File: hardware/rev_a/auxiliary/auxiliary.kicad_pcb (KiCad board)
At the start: 4 copper layers, 90 x 75 mm, 52 parts, among them J101 K1_NUMBERED_SOLDER_TAILS, J102 DEVKIT_J1_NUMBERED_TAILS, J103 ADAFRUIT_5335_TAILS, J104 B6B-XH-A(LF)(SN), J105 REGULATED_5V_TAILS, J106 REMOTE_NO_STOP_CONTACT, U101 ISO7721DR, U102 TXU0304PWR, U103 TXU0304PWR, U104 TXU0304PWR, U105 TPS3703A4330DSER, U106 TPS3703A4330DSER, U107 TPS3703A5500DSER, U108 TPS3703A5500DSER, U109 SN74LVC1G97DBVR, U110 SN74LVC1G97DBVR, U111 SN74LVC2G74DCUR

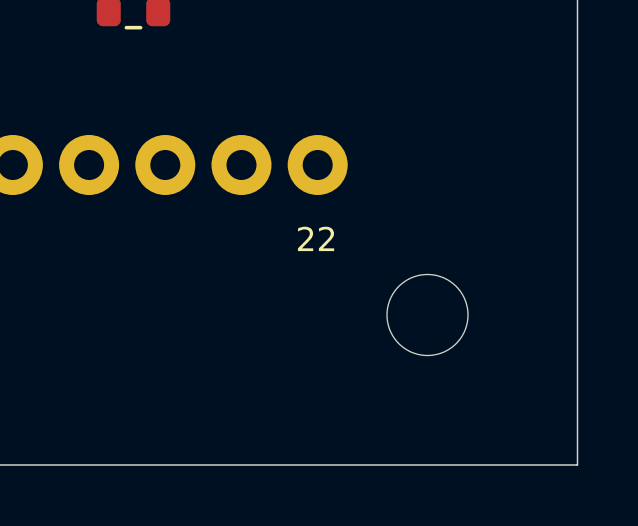
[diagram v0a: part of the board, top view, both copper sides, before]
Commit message: fix(hardware): move H4 clear of the unchanged MCU termination allocation
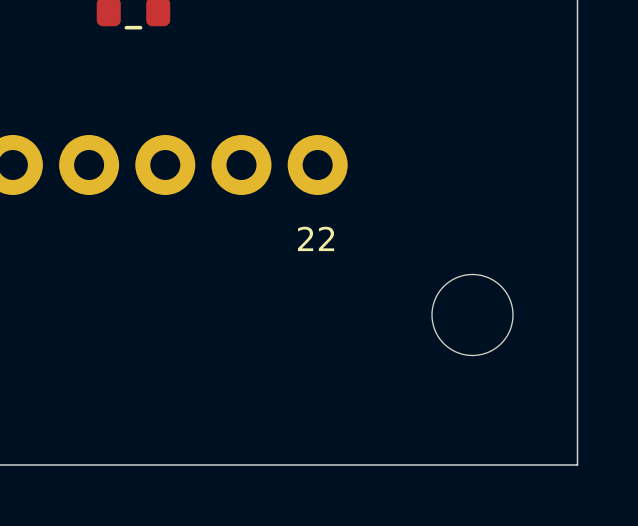
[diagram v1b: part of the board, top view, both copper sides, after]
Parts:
- moved H4 1.50 mm to (86.5, 70.0)
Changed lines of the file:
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@@
 	(footprint "MountingHole:MountingHole_2.7mm_M2.5"
 		(layer "F.Cu")
-		(at 85 70)
+		(at 86.5 70)
 		(descr "Mounting Hole 2.7mm, M2.5, no annular, generated by kicad-footprint-generator mountinghole.py")
 		(tags "mountinghole M2.5")

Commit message: feat(hardware): connect isolated ground references and local supply bypasses
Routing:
- net TARGET_GND: track 0.00 -> 46.5 mm, vias 0 -> 37
- net MCU_3V3: track 0.00 -> 21.7 mm
- net AFE_DVDD: track 0.00 -> 6.34 mm
- net HOST_GND: track 0.00 -> 2.72 mm, vias 0 -> 2
- net HOST_3V3: track 0.00 -> 1.95 mm
- added copper zone on In1.Cu, net HOST_GND
- added copper zone on In1.Cu, net TARGET_GND
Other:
- board text added: "P2 PARTIAL ROUTING - NOT FOR FABRICATION"
- board text removed: "P1 PLACEMENT ONLY - NOT FOR FABRICATION"
